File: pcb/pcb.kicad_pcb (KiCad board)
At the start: 2 copper layers, 1 part, among them U1 NodeMCU1.0(ESP-12E)

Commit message: First PCB revision complete
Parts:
- added R1: 10K, Resistor_THT:R_Axial_DIN0204_L3.6mm_D1.6mm_P7.62mm_Horizontal, B.Cu at (160.0, 92.7)
- added U2: DHT22, Connector_PinSocket_2.54mm:PinSocket_1x04_P2.54mm_Horizontal, B.Cu at (147.3, 100.3)
- added U3: SSD1306_OLED_128x32, personal:SSD1306_OLED_128x32, F.Cu at (175.3, 78.7)
- added U4: VL6180X_Adafruit, personal:VL6180X_Adafruit, B.Cu at (158.8, 104.1)
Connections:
- U1 pad 10: Net-(U1-Pad10) -> GND
- U1 pad 11: Net-(U1-Pad11) -> 3v3
- U1 pad 16: Net-(U1-Pad16) -> 3v3
- U1 pad 17: Net-(U1-Pad17) -> GND
- U1 pad 24: Net-(U1-Pad24) -> GND
- U1 pad 25: Net-(U1-Pad25) -> 3v3
- U1 pad 28: Net-(U1-Pad28) -> SDA
- U1 pad 29: Net-(U1-Pad29) -> SCL
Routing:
- net 3v3: track 0.00 -> 91.5 mm, vias 0 -> 2
- net GND: track 0.00 -> 58.3 mm, vias 0 -> 1
- net SDA: track 0.00 -> 33.5 mm
- net SCL: track 0.00 -> 33.5 mm
- net Net-(R1-Pad2): track 0.00 -> 28.0 mm

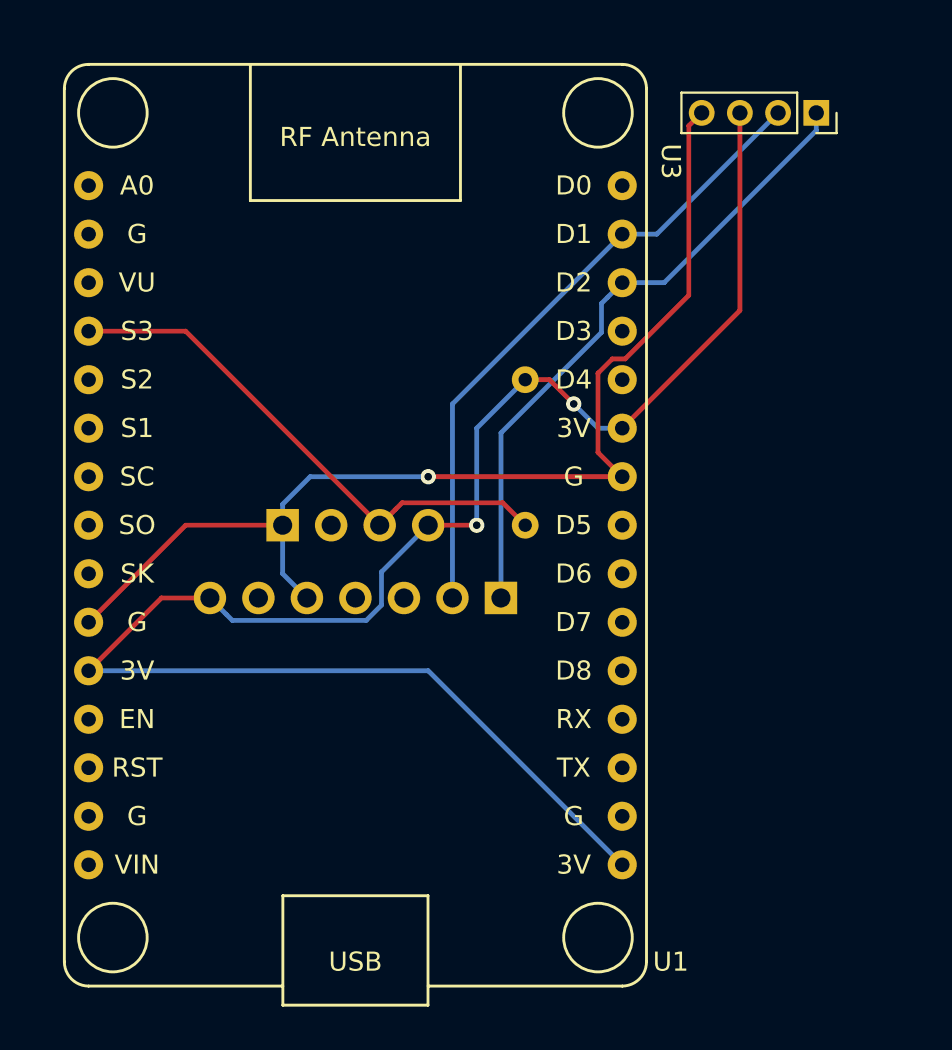
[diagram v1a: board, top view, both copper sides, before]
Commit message: Add board outline
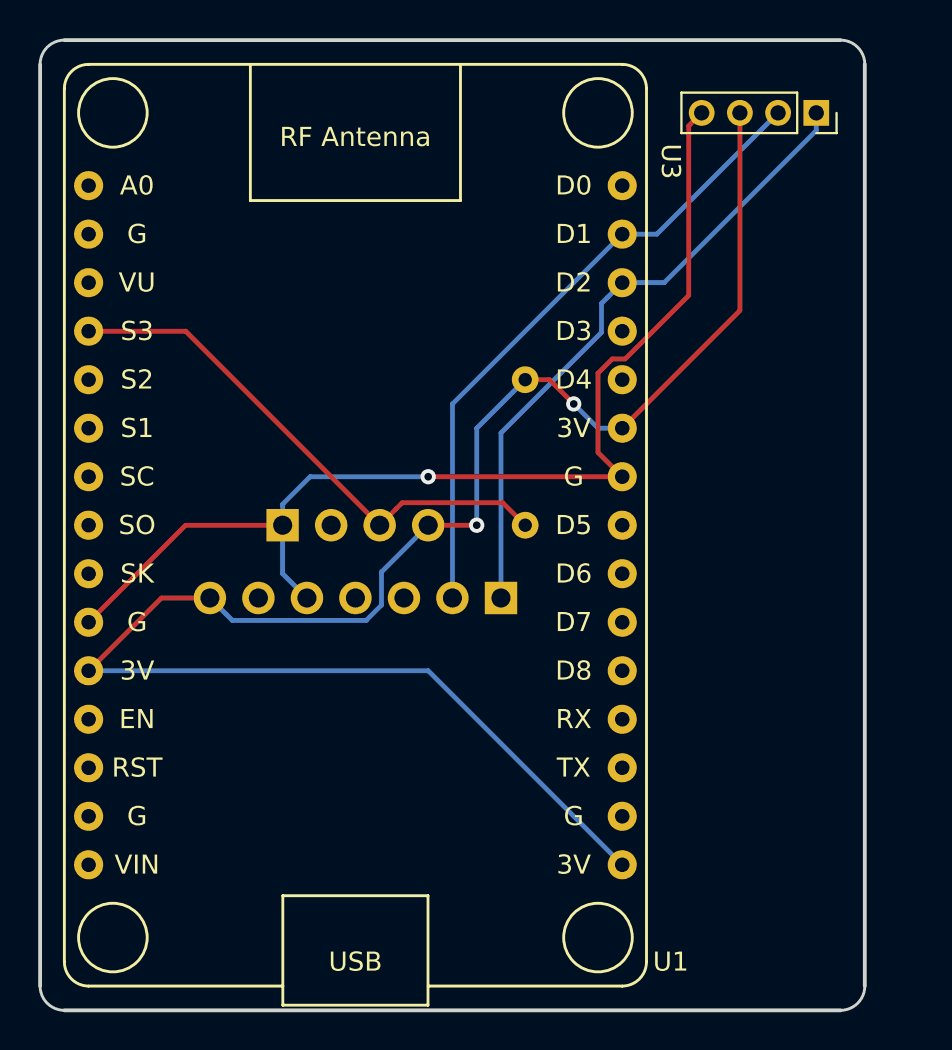
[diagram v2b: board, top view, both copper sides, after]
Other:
- board outline added: 43.2 x 50.8 mm
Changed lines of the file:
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@@
   (general
     (thickness 1.6)
-    (drawings 0)
+    (drawings 8)
     (tracks 55)
     (zones 0)
@@
       (net 21 "Net-(U1-Pad30)"))
   )
+  (gr_arc (start 176.53 124.46) (end 176.53 125.73) (angle -90) (layer Edge.Cuts) (width 0.15))
+  (gr_arc (start 135.89 124.46) (end 134.62 124.46) (angle -90) (layer Edge.Cuts) (width 0.15))
+  (gr_arc (start 135.89 76.2) (end 135.89 74.93) (angle -90) (layer Edge.Cuts) (width 0.15))
+  (gr_arc (start 176.53 76.2) (end 177.8 76.2) (angle -90) (layer Edge.Cuts) (width 0.15))
+  (gr_line (start 134.62 124.46) (end 134.62 76.2) (layer Edge.Cuts) (width 0.2))
+  (gr_line (start 176.53 125.73) (end 135.89 125.73) (layer Edge.Cuts) (width 0.2))
+  (gr_line (start 177.8 76.2) (end 177.8 124.46) (layer Edge.Cuts) (width 0.2))
+  (gr_line (start 135.89 74.93) (end 176.53 74.93) (layer Edge.Cuts) (width 0.2))
   (segment (start 167.295 87.63) (end 175.26 79.665) (width 0.25) (layer B.Cu) (net 23))
   (segment (start 175.26 79.665) (end 175.26 78.74) (width 0.25) (layer B.Cu) (net 23))

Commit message: Move sensors down; fix routing
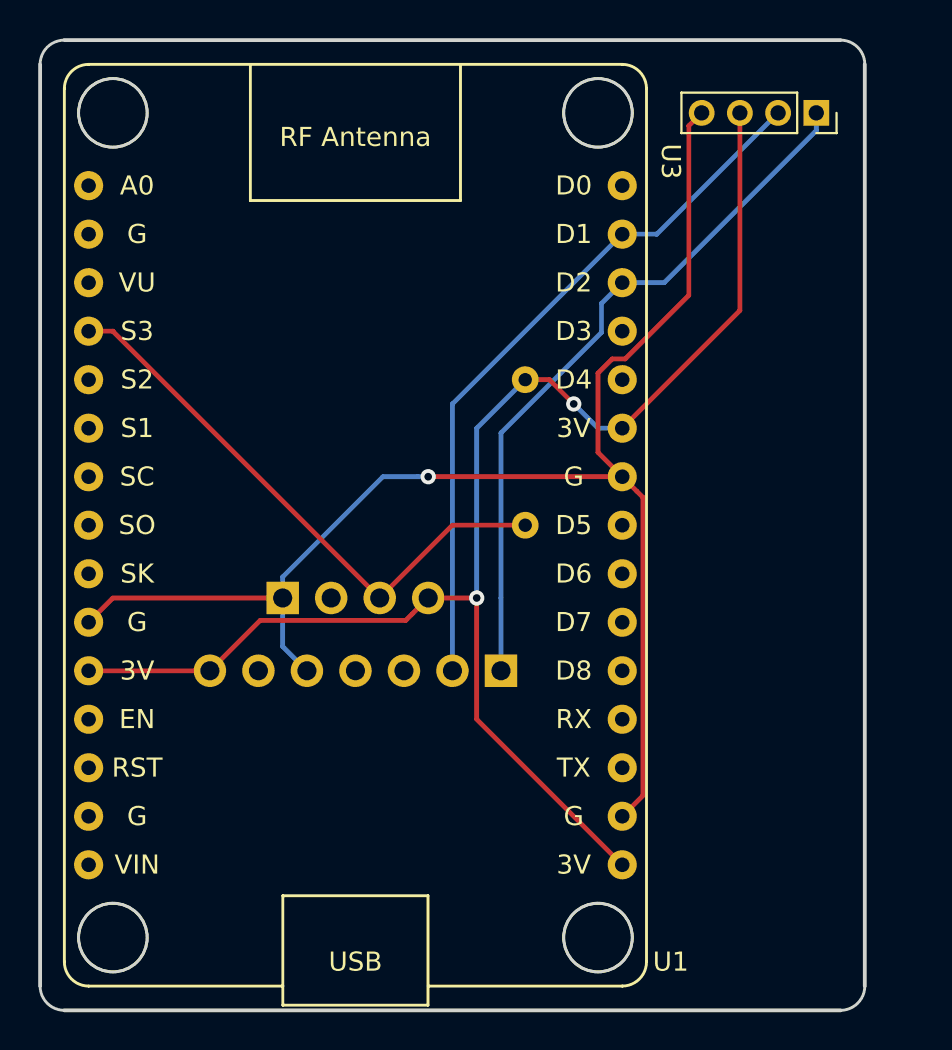
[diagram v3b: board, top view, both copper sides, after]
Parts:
- moved U2 3.81 mm to (147.3, 104.1)
- moved U4 3.81 mm to (158.8, 108.0)
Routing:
- net GND: track 58.3 -> 77.0 mm
- net 3v3: track 91.5 -> 76.7 mm
- net SDA: track 33.5 -> 37.3 mm
- net SCL: track 33.5 -> 37.3 mm
- net Net-(R1-Pad2): track 28.0 -> 30.2 mm
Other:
- outline, holes or cut-outs redrawn
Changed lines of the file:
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@@
   (general
     (thickness 1.6)
-    (drawings 8)
-    (tracks 55)
+    (drawings 12)
+    (tracks 57)
     (zones 0)
     (modules 5)
@@
   )
   (module personal:VL6180X_Adafruit (layer B.Cu)
-    (at 158.75 104.14 90)
+    (at 158.75 107.95 90)
     (descr "Through hole straight socket strip, 1x07, 2.54mm pitch, single row (from Kicad 4.0.7), script generated")
     (tags "Through hole socket strip THT 1x07 2.54mm single row")
@@
   )
   (module Connector_PinSocket_2.54mm:PinSocket_1x04_P2.54mm_Horizontal (layer B.Cu)
-    (at 147.32 100.33 270)
+    (at 147.32 104.14 270)
     (descr "Through hole angled socket strip, 1x04, 2.54mm pitch, 8.51mm socket length, single row (from Kicad 4.0.7), script generated")
     (tags "Through hole angled socket strip THT 1x04 2.54mm single row")
@@
       (effects (font (size 1 1) (thickness 0.15)))
     )
-    (fp_text value "NodeMCU1.0(ESP-12E)" (at 0 -25.4) (layer F.Fab)
+    (fp_text value "NodeMCU1.0(ESP-12E)" (at 0 -15.24) (layer F.Fab)
       (effects (font (size 1 1) (thickness 0.15)))
     )
@@
       (net 21 "Net-(U1-Pad30)"))
   )
+  (gr_circle (center 163.83 121.92) (end 165.1 120.65) (layer Edge.Cuts) (width 0.15))
+  (gr_circle (center 138.43 121.92) (end 139.7 120.65) (layer Edge.Cuts) (width 0.15))
+  (gr_circle (center 163.83 78.74) (end 165.1 77.47) (layer Edge.Cuts) (width 0.15))
+  (gr_circle (center 138.43 78.74) (end 139.7 77.47) (layer Edge.Cuts) (width 0.15))
   (gr_arc (start 176.53 124.46) (end 176.53 125.73) (angle -90) (layer Edge.Cuts) (width 0.15))
   (gr_arc (start 135.89 124.46) (end 134.62 124.46) (angle -90) (layer Edge.Cuts) (width 0.15))
@@
   (segment (start 175.26 79.665) (end 175.26 78.74) (width 0.25) (layer B.Cu) (net 23))
   (segment (start 165.1 87.63) (end 167.295 87.63) (width 0.25) (layer B.Cu) (net 23))
-  (segment (start 164.338001 88.391999) (end 165.1 87.63) (width 0.25) (layer B.Cu) (net 23))
-  (segment (start 164.012999 88.717001) (end 164.338001 88.391999) (width 0.25) (layer B.Cu) (net 23))
-  (segment (start 164.012999 90.234003) (end 164.012999 88.717001) (width 0.25) (layer B.Cu) (net 23))
-  (segment (start 158.75 95.497002) (end 164.012999 90.234003) (width 0.25) (layer B.Cu) (net 23))
-  (segment (start 158.75 104.14) (end 158.75 95.497002) (width 0.25) (layer B.Cu) (net 23))
+  (segment (start 158.75 104.14) (end 158.75 107.95) (width 0.25) (layer B.Cu) (net 23))
+  (segment (start 158.75 95.497002) (end 158.75 104.14) (width 0.25) (layer B.Cu) (net 23))
+  (segment (start 165.1 87.63) (end 164.012999 88.717001) (width 0.25) (layer B.Cu) (net 23))
+  (segment (start 164.012999 90.234003) (end 158.75 95.497002) (width 0.25) (layer B.Cu) (net 23))
+  (segment (start 164.012999 88.717001) (end 164.012999 90.234003) (width 0.25) (layer B.Cu) (net 23))
   (segment (start 156.21 93.98) (end 165.1 85.09) (width 0.25) (layer B.Cu) (net 24))
   (segment (start 156.21 104.14) (end 156.21 93.98) (width 0.25) (layer B.Cu) (net 24))
   (segment (start 166.91 85.09) (end 165.1 85.09) (width 0.25) (layer B.Cu) (net 24))
   (segment (start 173.26 78.74) (end 166.91 85.09) (width 0.25) (layer B.Cu) (net 24))
-  (segment (start 144.685001 105.315001) (end 144.359999 104.989999) (width 0.25) (layer B.Cu) (net 25))
-  (segment (start 151.694001 105.315001) (end 144.685001 105.315001) (width 0.25) (layer B.Cu) (net 25))
-  (segment (start 152.494999 104.514003) (end 151.694001 105.315001) (width 0.25) (layer B.Cu) (net 25))
-  (segment (start 152.494999 102.775001) (end 152.494999 104.514003) (width 0.25) (layer B.Cu) (net 25))
-  (segment (start 144.359999 104.989999) (end 143.51 104.14) (width 0.25) (layer B.Cu) (net 25))
-  (segment (start 154.94 100.33) (end 152.494999 102.775001) (width 0.25) (layer B.Cu) (net 25))
+  (segment (start 156.21 104.14) (end 156.21 107.95) (width 0.25) (layer B.Cu) (net 24))
   (segment (start 171.26 89.09) (end 165.1 95.25) (width 0.25) (layer F.Cu) (net 25))
   (segment (start 171.26 78.74) (end 171.26 89.09) (width 0.25) (layer F.Cu) (net 25))
-  (segment (start 140.97 104.14) (end 137.16 107.95) (width 0.25) (layer F.Cu) (net 25))
-  (segment (start 143.51 104.14) (end 140.97 104.14) (width 0.25) (layer F.Cu) (net 25))
   (via (at 162.56 93.98) (size 0.8) (drill 0.4) (layers F.Cu B.Cu) (net 25))
   (segment (start 160.02 92.71) (end 161.29 92.71) (width 0.25) (layer F.Cu) (net 25))
@@
   (segment (start 162.56 93.98) (end 163.83 95.25) (width 0.25) (layer B.Cu) (net 25))
   (segment (start 160.02 92.71) (end 157.48 95.25) (width 0.25) (layer B.Cu) (net 25))
-  (via (at 157.48 100.33) (size 0.8) (drill 0.4) (layers F.Cu B.Cu) (net 25))
+  (via (at 157.48 104.14) (size 0.8) (drill 0.4) (layers F.Cu B.Cu) (net 25))
   (segment (start 157.48 95.25) (end 157.48 100.33) (width 0.25) (layer B.Cu) (net 25))
-  (segment (start 157.48 100.33) (end 154.94 100.33) (width 0.25) (layer F.Cu) (net 25))
-  (segment (start 154.94 107.95) (end 165.1 118.11) (width 0.25) (layer B.Cu) (net 25))
-  (segment (start 137.16 107.95) (end 154.94 107.95) (width 0.25) (layer B.Cu) (net 25))
-  (segment (start 147.32 102.87) (end 148.59 104.14) (width 0.25) (layer B.Cu) (net 26))
-  (segment (start 147.32 100.33) (end 147.32 102.87) (width 0.25) (layer B.Cu) (net 26))
+  (segment (start 137.16 107.95) (end 143.51 107.95) (width 0.25) (layer F.Cu) (net 25))
+  (segment (start 157.48 110.49) (end 165.1 118.11) (width 0.25) (layer F.Cu) (net 25))
+  (segment (start 157.48 104.14) (end 154.94 104.14) (width 0.25) (layer F.Cu) (net 25))
+  (segment (start 154.090001 104.989999) (end 154.94 104.14) (width 0.25) (layer F.Cu) (net 25))
+  (segment (start 153.764999 105.315001) (end 154.090001 104.989999) (width 0.25) (layer F.Cu) (net 25))
+  (segment (start 146.144999 105.315001) (end 153.764999 105.315001) (width 0.25) (layer F.Cu) (net 25))
+  (segment (start 143.51 107.95) (end 146.144999 105.315001) (width 0.25) (layer F.Cu) (net 25))
+  (segment (start 157.48 100.33) (end 157.48 104.14) (width 0.25) (layer B.Cu) (net 25))
+  (segment (start 157.48 104.14) (end 157.48 110.49) (width 0.25) (layer F.Cu) (net 25))
+  (segment (start 154.94 97.79) (end 165.1 97.79) (width 0.25) (layer F.Cu) (net 26))
+  (via (at 154.94 97.79) (size 0.8) (drill 0.4) (layers F.Cu B.Cu) (net 26))
   (segment (start 164.578239 91.622999) (end 163.83 92.371238) (width 0.25) (layer F.Cu) (net 26))
   (segment (start 168.585001 88.293761) (end 165.255763 91.622999) (width 0.25) (layer F.Cu) (net 26))
@@
   (segment (start 163.83 96.52) (end 165.1 97.79) (width 0.25) (layer F.Cu) (net 26))
   (segment (start 163.83 92.371238) (end 163.83 96.52) (width 0.25) (layer F.Cu) (net 26))
-  (segment (start 142.24 100.33) (end 137.16 105.41) (width 0.25) (layer F.Cu) (net 26))
-  (segment (start 147.32 100.33) (end 142.24 100.33) (width 0.25) (layer F.Cu) (net 26))
-  (via (at 154.94 97.79) (size 0.8) (drill 0.4) (layers F.Cu B.Cu) (net 26))
-  (segment (start 148.76 97.79) (end 154.94 97.79) (width 0.25) (layer B.Cu) (net 26))
-  (segment (start 147.32 100.33) (end 147.32 99.23) (width 0.25) (layer B.Cu) (net 26))
-  (segment (start 147.32 99.23) (end 148.76 97.79) (width 0.25) (layer B.Cu) (net 26))
-  (segment (start 154.94 97.79) (end 165.1 97.79) (width 0.25) (layer F.Cu) (net 26))
-  (segment (start 153.249999 99.480001) (end 152.4 100.33) (width 0.25) (layer F.Cu) (net 27))
-  (segment (start 153.575001 99.154999) (end 153.249999 99.480001) (width 0.25) (layer F.Cu) (net 27))
-  (segment (start 158.844999 99.154999) (end 153.575001 99.154999) (width 0.25) (layer F.Cu) (net 27))
-  (segment (start 160.02 100.33) (end 158.844999 99.154999) (width 0.25) (layer F.Cu) (net 27))
-  (segment (start 142.24 90.17) (end 137.16 90.17) (width 0.25) (layer F.Cu) (net 27))
-  (segment (start 152.4 100.33) (end 142.24 90.17) (width 0.25) (layer F.Cu) (net 27))
+  (segment (start 138.43 104.14) (end 147.32 104.14) (width 0.25) (layer F.Cu) (net 26))
+  (segment (start 137.16 105.41) (end 138.43 104.14) (width 0.25) (layer F.Cu) (net 26))
+  (segment (start 147.32 106.68) (end 148.59 107.95) (width 0.25) (layer B.Cu) (net 26))
+  (segment (start 147.32 104.14) (end 147.32 106.68) (width 0.25) (layer B.Cu) (net 26))
+  (segment (start 154.374315 97.79) (end 154.94 97.79) (width 0.25) (layer B.Cu) (net 26))
+  (segment (start 152.57 97.79) (end 154.374315 97.79) (width 0.25) (layer B.Cu) (net 26))
+  (segment (start 147.32 103.04) (end 152.57 97.79) (width 0.25) (layer B.Cu) (net 26))
+  (segment (start 147.32 104.14) (end 147.32 103.04) (width 0.25) (layer B.Cu) (net 26))
+  (segment (start 165.861999 98.551999) (end 165.1 97.79) (width 0.25) (layer F.Cu) (net 26))
+  (segment (start 166.187001 98.877001) (end 165.861999 98.551999) (width 0.25) (layer F.Cu) (net 26))
+  (segment (start 166.187001 114.482999) (end 166.187001 98.877001) (width 0.25) (layer F.Cu) (net 26))
+  (segment (start 165.1 115.57) (end 166.187001 114.482999) (width 0.25) (layer F.Cu) (net 26))
+  (segment (start 138.43 90.17) (end 152.4 104.14) (width 0.25) (layer F.Cu) (net 27))
+  (segment (start 137.16 90.17) (end 138.43 90.17) (width 0.25) (layer F.Cu) (net 27))
+  (segment (start 156.21 100.33) (end 160.02 100.33) (width 0.25) (layer F.Cu) (net 27))
+  (segment (start 152.4 104.14) (end 156.21 100.33) (width 0.25) (layer F.Cu) (net 27))
 )

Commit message: Add push button
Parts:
- added R2: 10K, Resistor_THT:R_Axial_DIN0204_L3.6mm_D1.6mm_P7.62mm_Horizontal, B.Cu at (168.6, 114.3)
- added SW1: SW_Push, Button_Switch_THT:SW_PUSH_6mm, F.Cu at (169.2, 118.1)
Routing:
- net Net-(R2-Pad1): track 0.00 -> 62.3 mm
- net GND: track 77.0 -> 88.6 mm
- net 3v3: track 76.7 -> 87.3 mm
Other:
- board text added: "JLAM V1.0 2020-05-12"

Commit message: Correct display footprint to right size
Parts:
- U3: footprint personal:SSD1306_OLED_128x32 -> personal:SSD1306_Adafruit_128x32
- moved U3 1.80 mm to (176.5, 77.5)
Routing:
- net SDA: track 37.3 -> 39.1 mm
- net SCL: track 37.3 -> 38.9 mm
- net 3v3: track 87.3 -> 88.7 mm
- net GND: track 88.6 -> 89.8 mm
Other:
- board size 43.2 x 50.8 mm -> 44.5 x 50.8 mm
